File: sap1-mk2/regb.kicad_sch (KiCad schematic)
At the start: 0 parts

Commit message: added A Register, B Register, Instruction Register, and Memory Address Register
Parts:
- added C15, C16, C17: 0.1μF, symbol Device:C_Small
- added D10, D11, D12, D13, D14, D15, D16, D17: RED, symbol Device:LED
- added R16, R17, R18, R19, R20, R21, R22, R23: 220, symbol Device:R
- added U10: 74LS245, symbol 74xx:74LS245
- added U11, U12: 74LS173, symbol 74xx:74LS173
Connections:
- new net: D15.1 (K), R21.1
- new net: D17.1 (K), R23.1
- new net: D13.1 (K), R19.1
- new net: D16.1 (K), R22.1
- new net: D11.1 (K), R17.1
- new net: D14.1 (K), R20.1
- new net: D12.1 (K), R18.1
- new net: D10.1 (K), R16.1
- new net +5V: C15.2, C16.2, C17.2, U10.1 (A->B), U10.20 (VCC), U11.16 (VCC), U12.16 (VCC)
- new net BUS_0: U10.11 (B7), U12.11 (D3)
- new net BUS_1: U10.12 (B6), U12.12 (D2)
- new net BUS_2: U10.13 (B5), U12.13 (D1)
- new net BUS_3: U10.14 (B4), U12.14 (D0)
- new net BUS_4: U10.15 (B3), U11.11 (D3)
- new net BUS_5: U10.16 (B2), U11.12 (D2)
- new net BUS_6: U10.17 (B1), U11.13 (D1)
- new net BUS_7: U10.18 (B0), U11.14 (D0)
- new net B_0: D17.2 (A), U10.9 (A7), U12.6 (Q3)
- new net B_1: D16.2 (A), U10.8 (A6), U12.5 (Q2)
- new net B_2: D15.2 (A), U10.7 (A5), U12.4 (Q1)
- new net B_3: D14.2 (A), U10.6 (A4), U12.3 (Q0)
- new net B_4: D13.2 (A), U10.5 (A3), U11.6 (Q3)
- new net B_5: D12.2 (A), U10.4 (A2), U11.5 (Q2)
- new net B_6: D11.2 (A), U10.3 (A1), U11.4 (Q1)
- new net B_7: D10.2 (A), U10.2 (A0), U11.3 (Q0)
- new net CLK: U11.7 (Cp), U12.7 (Cp)
- new net CLR: U11.15 (Mr), U12.15 (Mr)
- new net GND: C15.1, C16.1, C17.1, R16.2, R17.2, R18.2, R19.2, R20.2, R21.2, R22.2, R23.2, U10.10 (GND), U11.1 (Oe1), U11.2 (Oe2), U11.8 (GND), U12.1 (Oe1), U12.2 (Oe2), U12.8 (GND)
- new net ~{BI}: U11.10 (E2), U11.9 (E1), U12.10 (E2), U12.9 (E1)
- new net ~{BO}: U10.19 (CE)
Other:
- title: (none) -> B Register

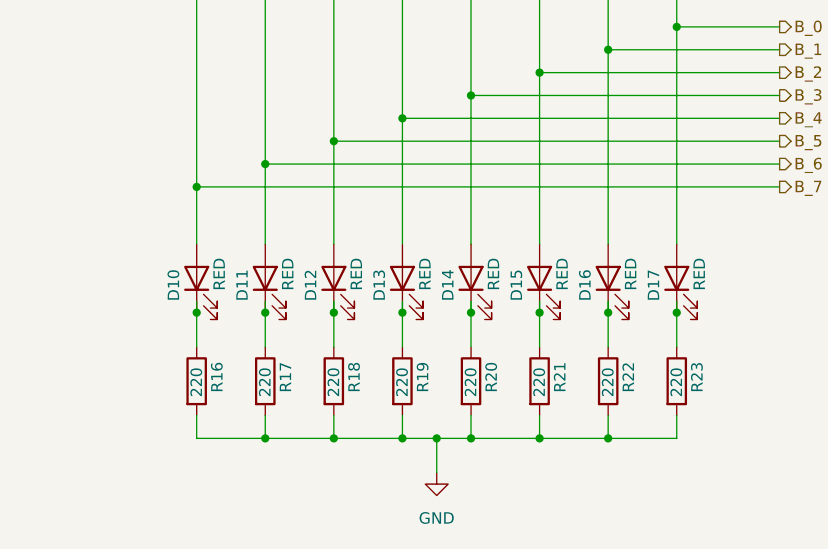
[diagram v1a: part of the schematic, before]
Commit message: added ALU + some minor tweaks
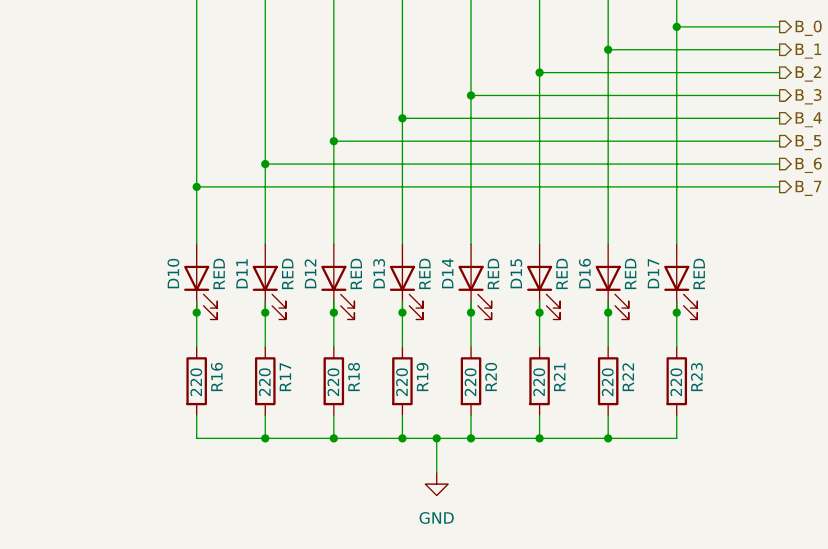
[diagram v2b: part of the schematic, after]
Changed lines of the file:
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@@
 		(dnp no)
 		(property "Reference" "D17"
-			(at 138.43 161.544 0)
+			(at 138.43 160.274 0)
 			(show_name no)
 			(do_not_autoplace no)
@@
 		(dnp no)
 		(property "Reference" "D13"
-			(at 107.95 161.544 0)
+			(at 107.95 160.274 0)
 			(show_name no)
 			(do_not_autoplace no)
@@
 		(dnp no)
 		(property "Reference" "D11"
-			(at 92.71 161.544 0)
+			(at 92.71 160.274 0)
 			(show_name no)
 			(do_not_autoplace no)
@@
 		(dnp no)
 		(property "Reference" "D15"
-			(at 123.19 161.544 0)
+			(at 123.19 160.274 0)
 			(show_name no)
 			(do_not_autoplace no)
@@
 		(dnp no)
 		(property "Reference" "D16"
-			(at 130.81 161.544 0)
+			(at 130.81 160.274 0)
 			(show_name no)
 			(do_not_autoplace no)
@@
 		(dnp no)
 		(property "Reference" "D14"
-			(at 115.57 161.544 0)
+			(at 115.57 160.274 0)
 			(show_name no)
 			(do_not_autoplace no)
@@
 		(dnp no)
 		(property "Reference" "D12"
-			(at 100.33 161.544 0)
+			(at 100.33 160.274 0)
 			(show_name no)
 			(do_not_autoplace no)
@@
 		(dnp no)
 		(property "Reference" "D10"
-			(at 85.09 161.544 0)
-			(show_name no)
-			(do_not_autoplace no)
+			(at 85.09 160.274 0)
+			(show_name no)
+			(do_not_autoplace no)
